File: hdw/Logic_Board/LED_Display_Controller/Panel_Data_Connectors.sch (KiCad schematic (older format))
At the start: 16 parts, among them J2901 STRING 1, J2902 STRING 2, J2903 STRING 3, J2904 STRING 4

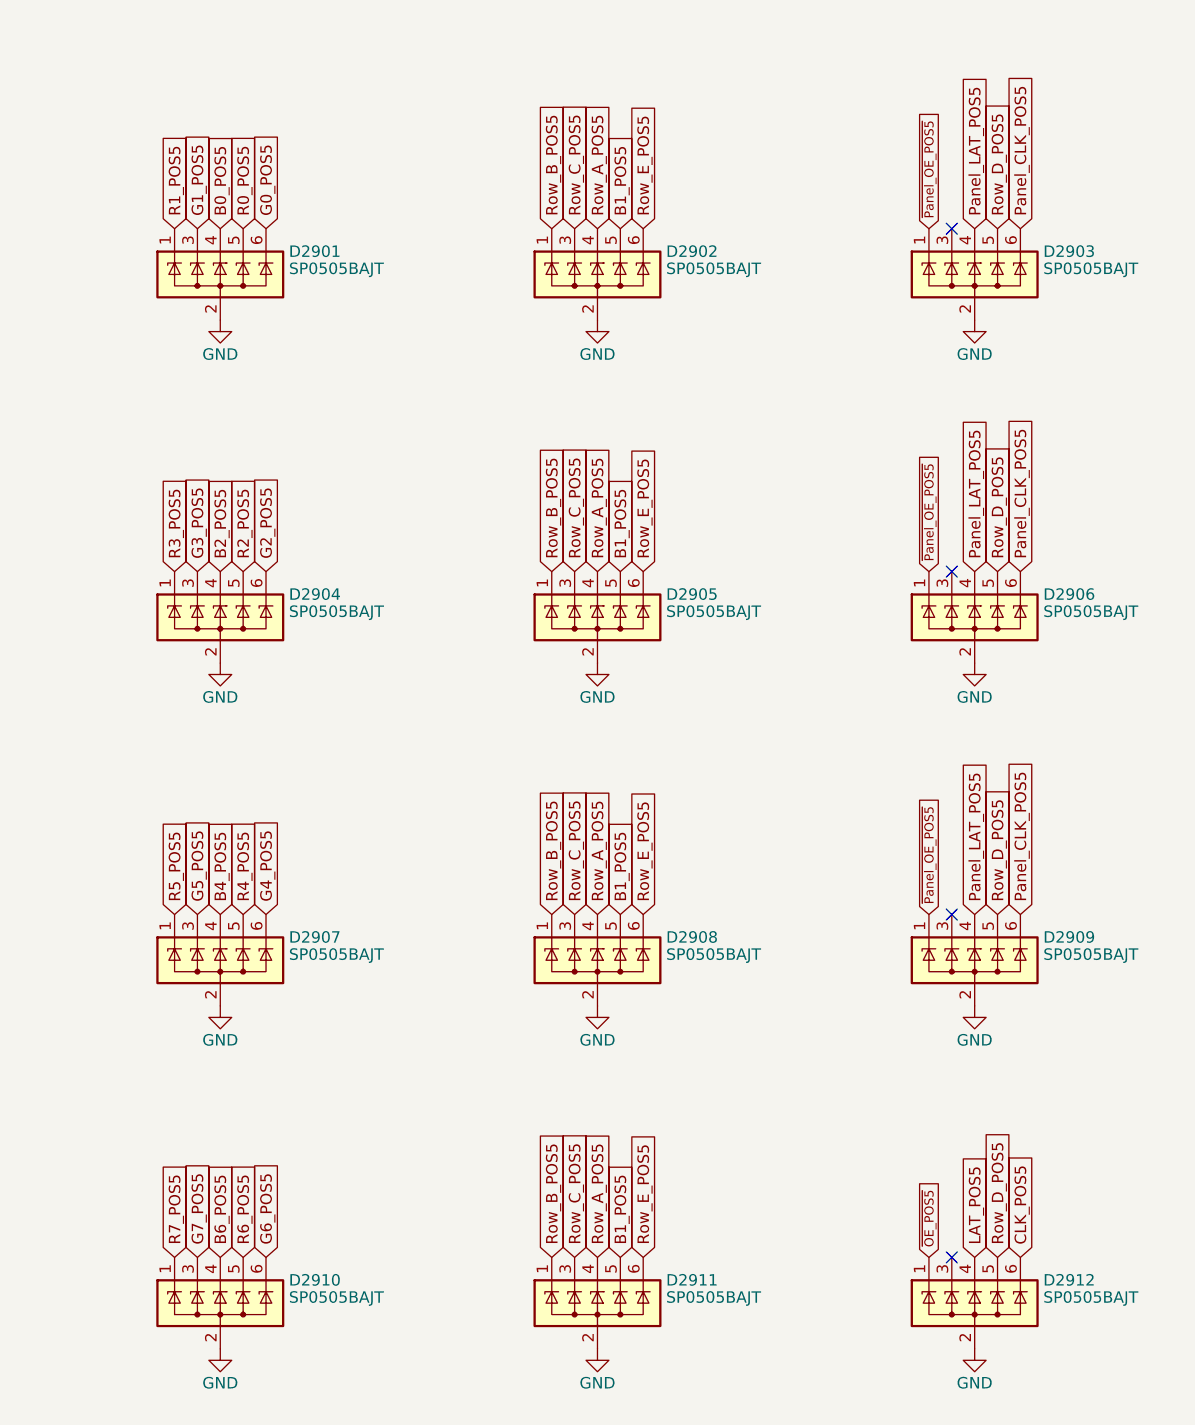
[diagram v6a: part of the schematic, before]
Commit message: Resolved panel data connector orientation issues
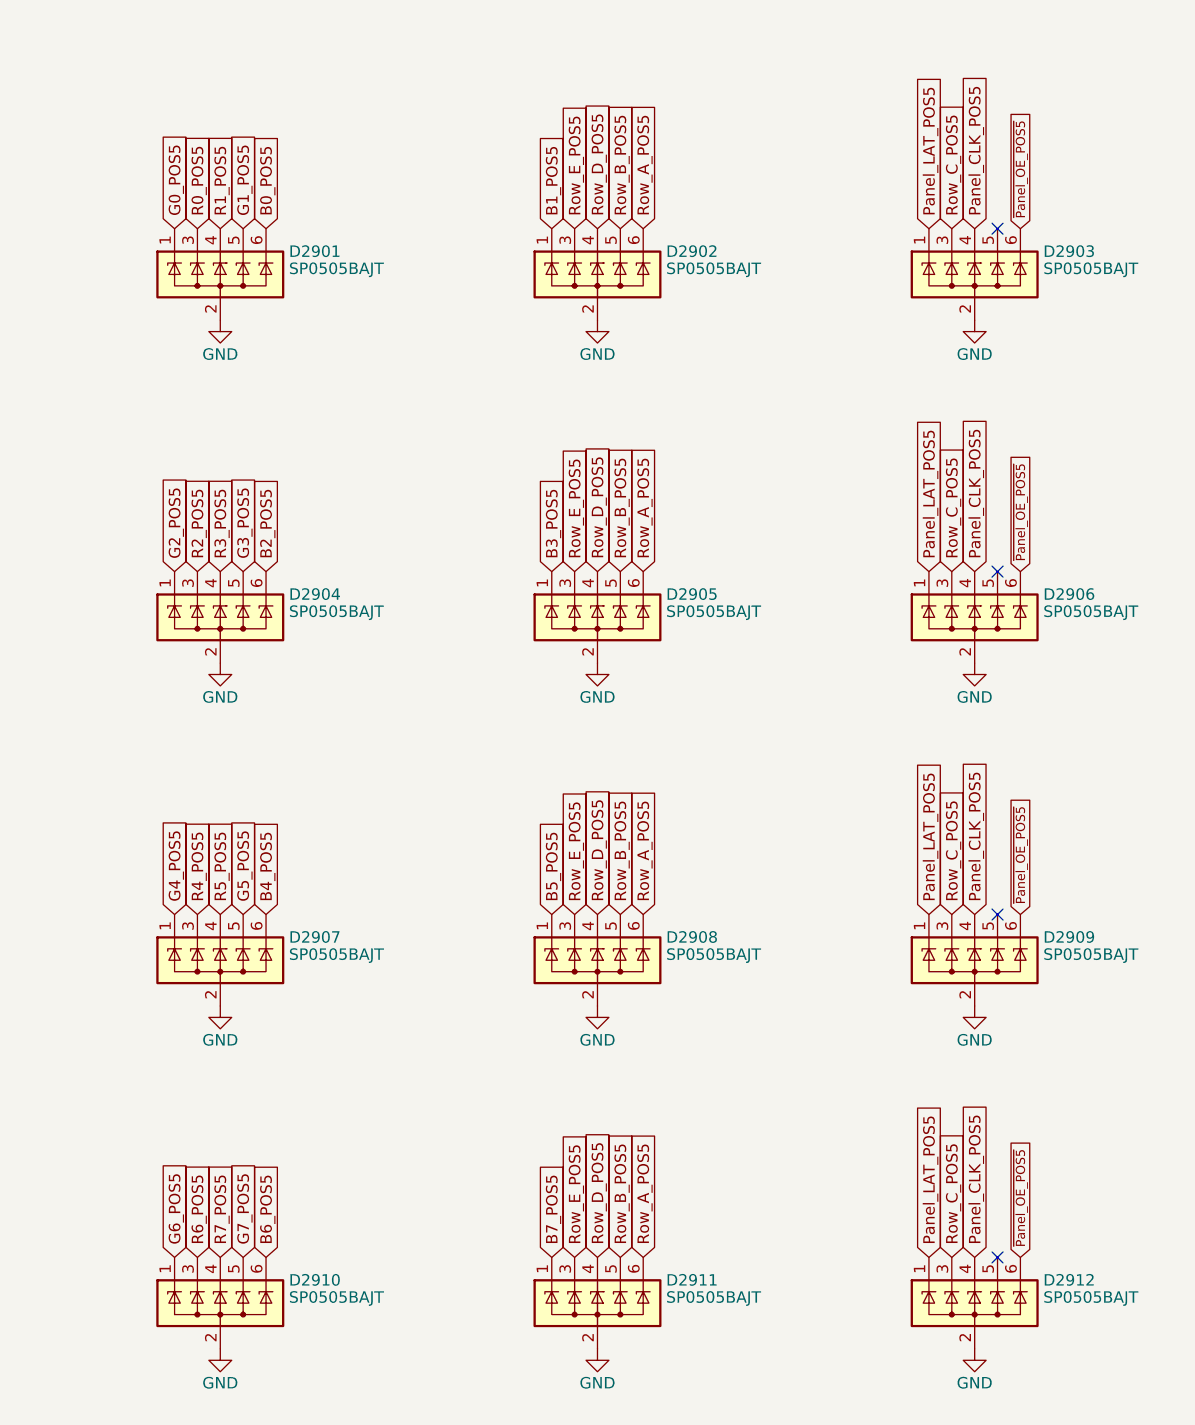
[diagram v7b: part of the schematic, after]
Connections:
- net CLK_POS5 is gone; now on net ~Panel_OE_POS5: D2912.6 (K)
- net LAT_POS5 is gone; now on net Panel_CLK_POS5: D2912.4 (K)
- net ~OE_POS5 is gone; now on net Panel_LAT_POS5: D2912.1 (K)
- net B0_POS5: now also D2901.6 (K); no longer D2901.4 (K)
- net B1_POS5: now also D2902.1 (K); no longer D2902.5 (K), D2905.5 (K), D2908.5 (K), D2911.5 (K)
- net B2_POS5: now also D2904.6 (K); no longer D2904.4 (K)
- net B3_POS5: now also D2905.1 (K)
- net B4_POS5: now also D2907.6 (K); no longer D2907.4 (K)
- net B5_POS5: now also D2908.1 (K)
- net B6_POS5: now also D2910.6 (K); no longer D2910.4 (K)
- net B7_POS5: now also D2911.1 (K)
- net G0_POS5: now also D2901.1 (K); no longer D2901.6 (K)
- net G1_POS5: now also D2901.5 (K); no longer D2901.3 (K)
- net G2_POS5: now also D2904.1 (K); no longer D2904.6 (K)
- net G3_POS5: now also D2904.5 (K); no longer D2904.3 (K)
- net G4_POS5: now also D2907.1 (K); no longer D2907.6 (K)
- net G5_POS5: now also D2907.5 (K); no longer D2907.3 (K)
- net G6_POS5: now also D2910.1 (K); no longer D2910.6 (K)
- net G7_POS5: now also D2910.5 (K); no longer D2910.3 (K)
- net Panel_CLK_POS5: now also D2903.4 (K), D2906.4 (K), D2909.4 (K); no longer D2903.6 (K), D2906.6 (K), D2909.6 (K)
- net Panel_LAT_POS5: now also D2903.1 (K), D2906.1 (K), D2909.1 (K); no longer D2903.4 (K), D2906.4 (K), D2909.4 (K)
- net R0_POS5: now also D2901.3 (K); no longer D2901.5 (K)
- net R1_POS5: now also D2901.4 (K); no longer D2901.1 (K)
- net R2_POS5: now also D2904.3 (K); no longer D2904.5 (K)
- net R3_POS5: now also D2904.4 (K); no longer D2904.1 (K)
- net R4_POS5: now also D2907.3 (K); no longer D2907.5 (K)
- net R5_POS5: now also D2907.4 (K); no longer D2907.1 (K)
- net R6_POS5: now also D2910.3 (K); no longer D2910.5 (K)
- net R7_POS5: now also D2910.4 (K); no longer D2910.1 (K)
- net Row_A_POS5: now also D2902.6 (K), D2905.6 (K), D2908.6 (K), D2911.6 (K); no longer D2902.4 (K), D2905.4 (K), D2908.4 (K), D2911.4 (K)
- net Row_B_POS5: now also D2902.5 (K), D2905.5 (K), D2908.5 (K), D2911.5 (K); no longer D2902.1 (K), D2905.1 (K), D2908.1 (K), D2911.1 (K)
- net Row_C_POS5: now also D2903.3 (K), D2906.3 (K), D2909.3 (K), D2912.3 (K); no longer D2902.3 (K), D2905.3 (K), D2908.3 (K), D2911.3 (K)
- net Row_D_POS5: now also D2902.4 (K), D2905.4 (K), D2908.4 (K), D2911.4 (K); no longer D2903.5 (K), D2906.5 (K), D2909.5 (K), D2912.5 (K)
- net Row_E_POS5: now also D2902.3 (K), D2905.3 (K), D2908.3 (K), D2911.3 (K); no longer D2902.6 (K), D2905.6 (K), D2908.6 (K), D2911.6 (K)
- net ~Panel_OE_POS5: now also D2903.6 (K), D2906.6 (K), D2909.6 (K); no longer D2903.1 (K), D2906.1 (K), D2909.1 (K)
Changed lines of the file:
@@
 Text GLabel 2850 5970 2    50   Input ~ 0
 G7_POS5
+Text GLabel 6780 1450 1    50   Input ~ 0
+Row_A_POS5
+Text GLabel 8130 1450 1    50   Input ~ 0
+Row_C_POS5
+Text GLabel 4830 1450 1    50   Input ~ 0
+R0_POS5
+Text GLabel 5130 1450 1    50   Input ~ 0
+B0_POS5
+Text GLabel 4930 1450 1    50   Input ~ 0
+R1_POS5
+Text GLabel 6380 1450 1    50   Input ~ 0
+B1_POS5
+Text GLabel 8230 1450 1    50   Input ~ 0
+Panel_CLK_POS5
+Text GLabel 8430 1450 1    40   Input ~ 0
+~Panel_OE_POS5
+Text GLabel 6680 1450 1    50   Input ~ 0
+Row_B_POS5
 Text GLabel 6580 1450 1    50   Input ~ 0
-Row_A_POS5
+Row_D_POS5
 Text GLabel 6480 1450 1    50   Input ~ 0
-Row_C_POS5
+Row_E_POS5
+Text GLabel 8030 1450 1    50   Input ~ 0
+Panel_LAT_POS5
+Text GLabel 4730 1450 1    50   Input ~ 0
+G0_POS5
 Text GLabel 5030 1450 1    50   Input ~ 0
-R0_POS5
-Text GLabel 4930 1450 1    50   Input ~ 0
-B0_POS5
-Text GLabel 4730 1450 1    50   Input ~ 0
-R1_POS5
-Text GLabel 6680 1450 1    50   Input ~ 0
-B1_POS5
-Text GLabel 8430 1450 1    50   Input ~ 0
-Panel_CLK_POS5
-Text GLabel 8030 1450 1    40   Input ~ 0
-~Panel_OE_POS5
-Text GLabel 6380 1450 1    50   Input ~ 0
-Row_B_POS5
-Text GLabel 8330 1450 1    50   Input ~ 0
-Row_D_POS5
-Text GLabel 6780 1450 1    50   Input ~ 0
-Row_E_POS5
-Text GLabel 8230 1450 1    50   Input ~ 0
-Panel_LAT_POS5
-Text GLabel 5130 1450 1    50   Input ~ 0
-G0_POS5
-Text GLabel 4830 1450 1    50   Input ~ 0
 G1_POS5
 Text Notes 2130 7740 0    50   ~ 0
@@
 	1    0    0    -1
 $EndComp
-NoConn ~ 8130 1450
-NoConn ~ 8130 2950
-NoConn ~ 8130 4450
-NoConn ~ 8130 5950
-Text GLabel 5030 2950 1    50   Input ~ 0
-R2_POS5
-Text GLabel 4930 2950 1    50   Input ~ 0
-B2_POS5
-Text GLabel 4730 2950 1    50   Input ~ 0
-R3_POS5
-Text GLabel 5130 2950 1    50   Input ~ 0
-G2_POS5
-Text GLabel 4830 2950 1    50   Input ~ 0
-G3_POS5
-Text GLabel 5030 4450 1    50   Input ~ 0
-R4_POS5
-Text GLabel 4930 4450 1    50   Input ~ 0
-B4_POS5
-Text GLabel 4730 4450 1    50   Input ~ 0
-R5_POS5
-Text GLabel 5130 4450 1    50   Input ~ 0
-G4_POS5
-Text GLabel 4830 4450 1    50   Input ~ 0
-G5_POS5
-Text GLabel 5030 5950 1    50   Input ~ 0
-R6_POS5
-Text GLabel 4930 5950 1    50   Input ~ 0
-B6_POS5
-Text GLabel 4730 5950 1    50   Input ~ 0
-R7_POS5
-Text GLabel 5130 5950 1    50   Input ~ 0
-G6_POS5
-Text GLabel 4830 5950 1    50   Input ~ 0
-G7_POS5
-Text GLabel 6580 2950 1    50   Input ~ 0
-Row_A_POS5
-Text GLabel 6480 2950 1    50   Input ~ 0
-Row_C_POS5
-Text GLabel 6680 2950 1    50   Input ~ 0
-B1_POS5
-Text GLabel 6380 2950 1    50   Input ~ 0
-Row_B_POS5
-Text GLabel 6780 2950 1    50   Input ~ 0
-Row_E_POS5
-Text GLabel 6580 4450 1    50   Input ~ 0
-Row_A_POS5
-Text GLabel 6480 4450 1    50   Input ~ 0
-Row_C_POS5
-Text GLabel 6680 4450 1    50   Input ~ 0
-B1_POS5
-Text GLabel 6380 4450 1    50   Input ~ 0
-Row_B_POS5
-Text GLabel 6780 4450 1    50   Input ~ 0
-Row_E_POS5
-Text GLabel 6580 5950 1    50   Input ~ 0
-Row_A_POS5
-Text GLabel 6480 5950 1    50   Input ~ 0
-Row_C_POS5
-Text GLabel 6680 5950 1    50   Input ~ 0
-B1_POS5
-Text GLabel 6380 5950 1    50   Input ~ 0
-Row_B_POS5
-Text GLabel 6780 5950 1    50   Input ~ 0
-Row_E_POS5
-Text GLabel 8430 2950 1    50   Input ~ 0
-Panel_CLK_POS5
-Text GLabel 8030 2950 1    40   Input ~ 0
-~Panel_OE_POS5
-Text GLabel 8330 2950 1    50   Input ~ 0
-Row_D_POS5
-Text GLabel 8230 2950 1    50   Input ~ 0
-Panel_LAT_POS5
-Text GLabel 8430 4450 1    50   Input ~ 0
-Panel_CLK_POS5
-Text GLabel 8030 4450 1    40   Input ~ 0
-~Panel_OE_POS5
-Text GLabel 8330 4450 1    50   Input ~ 0
-Row_D_POS5
-Text GLabel 8230 4450 1    50   Input ~ 0
-Panel_LAT_POS5
-Text GLabel 8430 5950 1    50   Input ~ 0
-CLK_POS5
-Text GLabel 8030 5950 1    40   Input ~ 0
-~OE_POS5
-Text GLabel 8330 5950 1    50   Input ~ 0
-Row_D_POS5
-Text GLabel 8230 5950 1    50   Input ~ 0
-LAT_POS5
 Wire Wire Line
 	2850 1970 3650 1970
@@
 Wire Wire Line
 	2850 5870 3650 5870
+NoConn ~ 8330 1450
+Text GLabel 6780 2950 1    50   Input ~ 0
+Row_A_POS5
+Text GLabel 8130 2950 1    50   Input ~ 0
+Row_C_POS5
+Text GLabel 4830 2950 1    50   Input ~ 0
+R2_POS5
+Text GLabel 5130 2950 1    50   Input ~ 0
+B2_POS5
+Text GLabel 4930 2950 1    50   Input ~ 0
+R3_POS5
+Text GLabel 6380 2950 1    50   Input ~ 0
+B3_POS5
+Text GLabel 8230 2950 1    50   Input ~ 0
+Panel_CLK_POS5
+Text GLabel 8430 2950 1    40   Input ~ 0
+~Panel_OE_POS5
+Text GLabel 6680 2950 1    50   Input ~ 0
+Row_B_POS5
+Text GLabel 6580 2950 1    50   Input ~ 0
+Row_D_POS5
+Text GLabel 6480 2950 1    50   Input ~ 0
+Row_E_POS5
+Text GLabel 8030 2950 1    50   Input ~ 0
+Panel_LAT_POS5
+Text GLabel 4730 2950 1    50   Input ~ 0
+G2_POS5
+Text GLabel 5030 2950 1    50   Input ~ 0
+G3_POS5
+NoConn ~ 8330 2950
+Text GLabel 6780 4450 1    50   Input ~ 0
+Row_A_POS5
+Text GLabel 8130 4450 1    50   Input ~ 0
+Row_C_POS5
+Text GLabel 4830 4450 1    50   Input ~ 0
+R4_POS5
+Text GLabel 5130 4450 1    50   Input ~ 0
+B4_POS5
+Text GLabel 4930 4450 1    50   Input ~ 0
+R5_POS5
+Text GLabel 6380 4450 1    50   Input ~ 0
+B5_POS5
+Text GLabel 8230 4450 1    50   Input ~ 0
+Panel_CLK_POS5
+Text GLabel 8430 4450 1    40   Input ~ 0
+~Panel_OE_POS5
+Text GLabel 6680 4450 1    50   Input ~ 0
+Row_B_POS5
+Text GLabel 6580 4450 1    50   Input ~ 0
+Row_D_POS5
+Text GLabel 6480 4450 1    50   Input ~ 0
+Row_E_POS5
+Text GLabel 8030 4450 1    50   Input ~ 0
+Panel_LAT_POS5
+Text GLabel 4730 4450 1    50   Input ~ 0
+G4_POS5
+Text GLabel 5030 4450 1    50   Input ~ 0
+G5_POS5
+NoConn ~ 8330 4450
+Text GLabel 6780 5950 1    50   Input ~ 0
+Row_A_POS5
+Text GLabel 8130 5950 1    50   Input ~ 0
+Row_C_POS5
+Text GLabel 4830 5950 1    50   Input ~ 0
+R6_POS5
+Text GLabel 5130 5950 1    50   Input ~ 0
+B6_POS5
+Text GLabel 4930 5950 1    50   Input ~ 0
+R7_POS5
+Text GLabel 6380 5950 1    50   Input ~ 0
+B7_POS5
+Text GLabel 8230 5950 1    50   Input ~ 0
+Panel_CLK_POS5
+Text GLabel 8430 5950 1    40   Input ~ 0
+~Panel_OE_POS5
+Text GLabel 6680 5950 1    50   Input ~ 0
+Row_B_POS5
+Text GLabel 6580 5950 1    50   Input ~ 0
+Row_D_POS5
+Text GLabel 6480 5950 1    50   Input ~ 0
+Row_E_POS5
+Text GLabel 8030 5950 1    50   Input ~ 0
+Panel_LAT_POS5
+Text GLabel 4730 5950 1    50   Input ~ 0
+G6_POS5
+Text GLabel 5030 5950 1    50   Input ~ 0
+G7_POS5
+NoConn ~ 8330 5950
 $EndSCHEMATC
